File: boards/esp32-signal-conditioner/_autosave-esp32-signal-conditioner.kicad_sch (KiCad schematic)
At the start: 5 parts

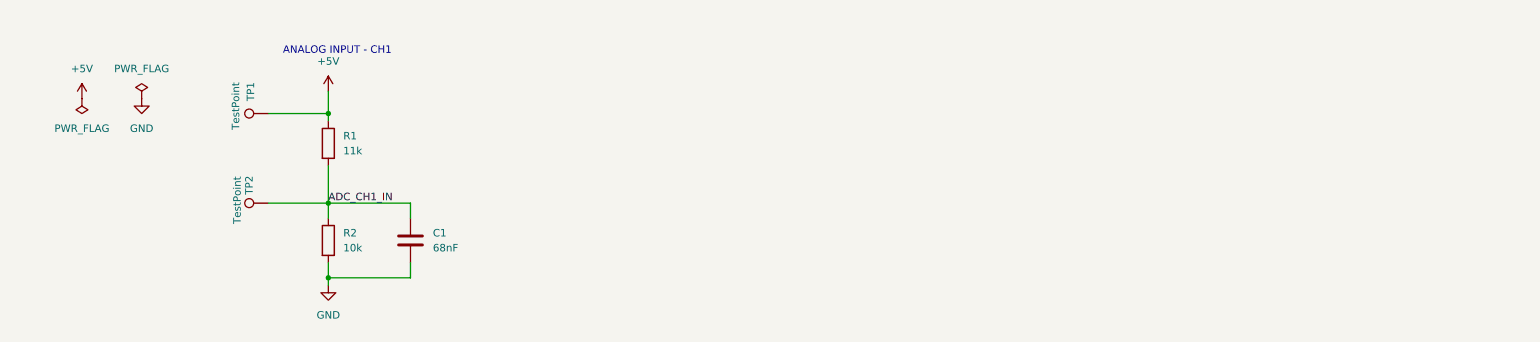
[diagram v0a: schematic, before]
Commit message: Add Ch2 Ch3 Ch4 analog input channels, all test points, ERC clean
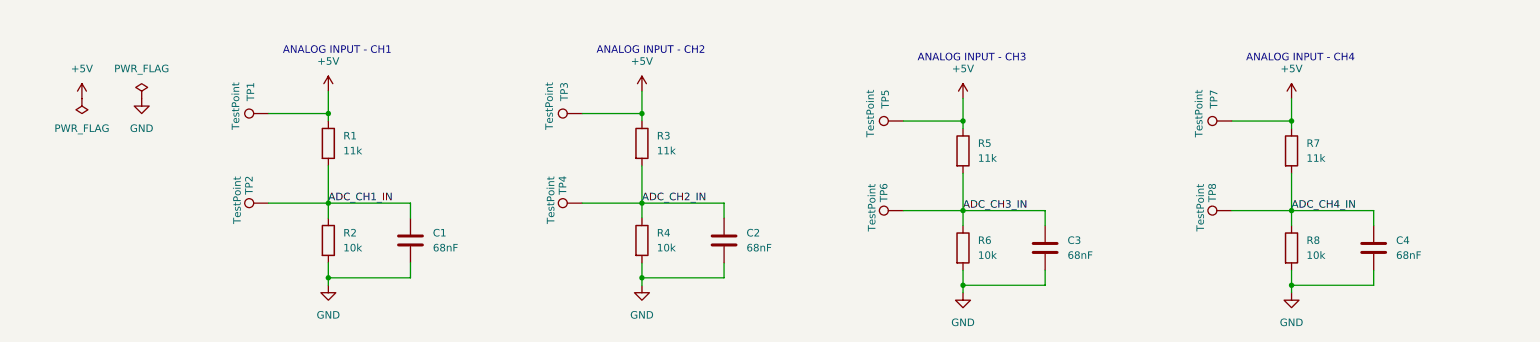
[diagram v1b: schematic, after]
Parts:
- added C2, C3, C4: 68nF, symbol Device:C
- added R3, R5, R7: 11k, symbol Device:R
- added R4, R6, R8: 10k, symbol Device:R
- added TP3, TP4, TP5, TP6, TP7, TP8: TestPoint, symbol Connector:TestPoint
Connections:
- net +5V: now also R3.1, R5.1, R7.1, TP3.1, TP5.1, TP7.1
- net GND: now also C2.2, C3.2, C4.2, R4.2, R6.2, R8.2
- new net ADC_CH2_IN: C2.1, R3.2, R4.1, TP4.1
- new net ADC_CH3_IN: C3.1, R5.2, R6.1, TP6.1
- new net ADC_CH4_IN: C4.1, R7.2, R8.1, TP8.1
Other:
- note added: "ANALOG INPUT - CH2"
- note added: "ANALOG INPUT - CH3"
- note added: "ANALOG INPUT - CH4"

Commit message: Add J1 input connector TBL002A 5-pos 3.5mm, footprint assigned, ERC clean
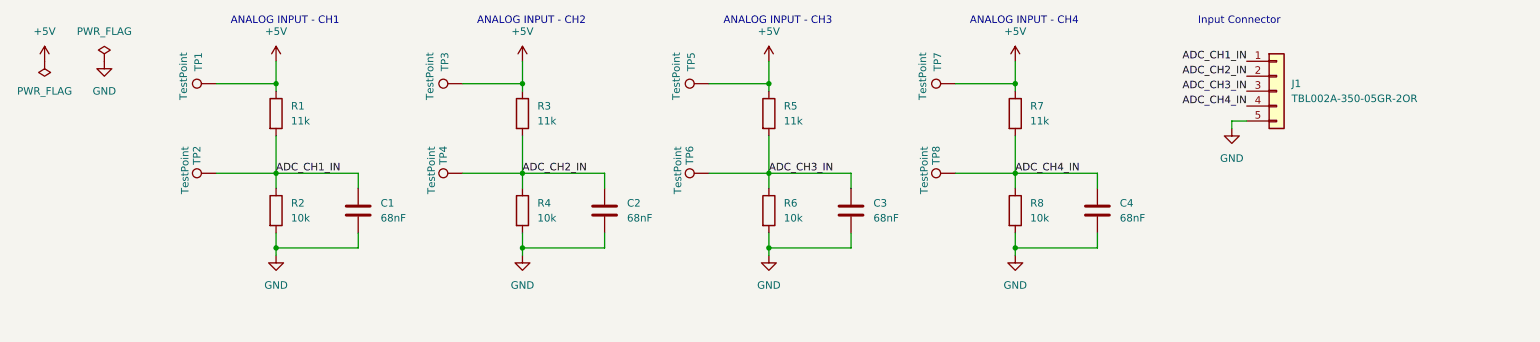
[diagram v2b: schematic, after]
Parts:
- added J1: TBL002A-350-05GR-2OR, TerminalBlock_Degson:TerminalBlock_Degson_DG250-3.5-05P_1x05_P3.50mm_45Degree, symbol Connector_Generic:Conn_01x05
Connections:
- net ADC_CH1_IN: now also J1.1 (Pin_1)
- net ADC_CH2_IN: now also J1.2 (Pin_2)
- net ADC_CH3_IN: now also J1.3 (Pin_3)
- net ADC_CH4_IN: now also J1.4 (Pin_4)
- net GND: now also J1.5 (Pin_5)
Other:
- note added: "Input Connector"
- moved on the sheet: C1, C2, C3, C4, R1, R2, R3, R4, R5, R6, R7, R8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

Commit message: Add C5 100nF and C6 10uF decoupling on +5V rail, ERC clean
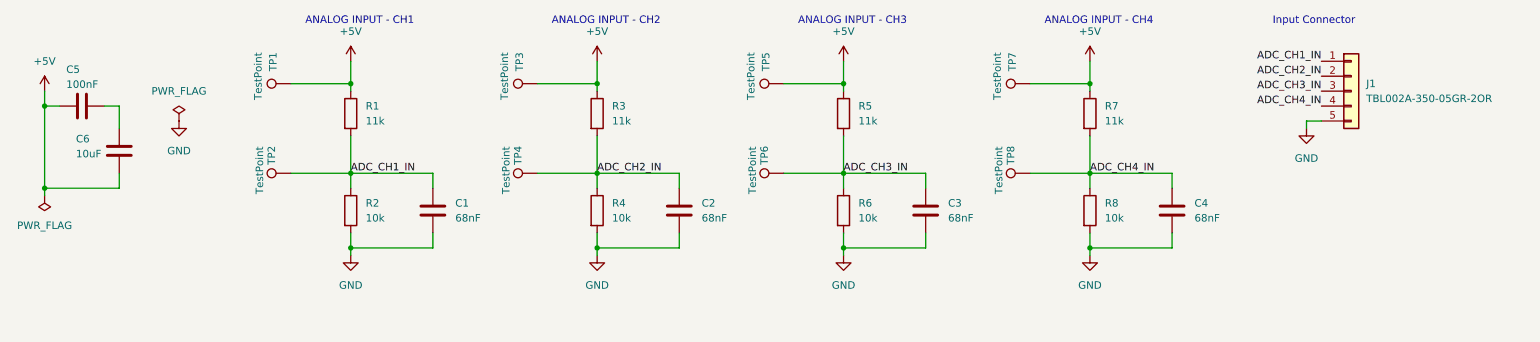
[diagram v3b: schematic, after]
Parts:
- added C5: 100nF, symbol Device:C
- added C6: 10uF, symbol Device:C
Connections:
- net +5V: now also C5.1, C6.2
- new net: C5.2, C6.1
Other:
- moved on the sheet: C1, C2, C3, C4, J1, R1, R2, R3, R4, R5, R6, R7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
